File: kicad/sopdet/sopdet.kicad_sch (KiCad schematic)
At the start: 0 parts

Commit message: Finish Sopdet schematic
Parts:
- added C1: 10u, Capacitor_SMD:C_0603_1608Metric_Pad1.08x0.95mm_HandSolder, symbol Device:C_Small
- added C10, C2, C3, C9: 0, Capacitor_SMD:C_0603_1608Metric, symbol Device:C_Small
- added C11, C12: 100p, Capacitor_SMD:C_0603_1608Metric, symbol Device:C_Small
- added C13, C15: 100n, Capacitor_SMD:C_0603_1608Metric, symbol Device:C_Small
- added C14: 10u, Capacitor_SMD:C_0603_1608Metric, symbol Device:C_Small
- added C16: 33p, Capacitor_SMD:C_0603_1608Metric, symbol Device:C_Small
- added C4: 100n, Capacitor_SMD:C_0603_1608Metric_Pad1.08x0.95mm_HandSolder, symbol Device:C_Small
- added C5: 47p, Capacitor_SMD:C_0603_1608Metric_Pad1.08x0.95mm_HandSolder, symbol Device:C_Small
- added C6, C7: 22u, Capacitor_SMD:C_1206_3216Metric, symbol Device:C_Small
- added C8: 1000u, Capacitor_SMD:CP_Elec_10x10.5, symbol Device:C_Polarized_Small
- added D1, D2: LED_Small, LED_SMD:LED_0603_1608Metric_Pad1.05x0.95mm_HandSolder, symbol Device:LED_Small
- added D3: TVS, Diode_SMD:D_SOD-882, symbol Diode:PTVS5V0Z1USK
- added D4: Blue LED, LED_SMD:LED_0603_1608Metric_Pad1.05x0.95mm_HandSolder, symbol Device:LED
- added D5: Yellow LED, LED_SMD:LED_0603_1608Metric_Pad1.05x0.95mm_HandSolder, symbol Device:LED
- added D6: Orange LED, LED_SMD:LED_0603_1608Metric_Pad1.05x0.95mm_HandSolder, symbol Device:LED
- added J1, J2: IPEX_MHF1, sirius:ipex_mhf1, symbol sirius:IPEX_MHF1
- added L1: 6.8u, sirius:1277AS-H-1R0M=P2, symbol Device:L_Small
- added L2: 68n, Inductor_SMD:L_0603_1608Metric, symbol Device:L_Small
- added Q1: Q_PMOS_GSD, sirius:SOT_7DS-T1-GE3_VIS, symbol Transistor_FET:Q_PMOS_GSD
- added R1, R5: 0, Resistor_SMD:R_0603_1608Metric, symbol Device:R_Small
- added R10, R7: 1k, Resistor_SMD:R_0603_1608Metric_Pad0.98x0.95mm_HandSolder, symbol Device:R_Small
- added R11, R12, R9: 1k, Resistor_SMD:R_0603_1608Metric, symbol Device:R_Small
- added R2: 2k, Resistor_SMD:R_0603_1608Metric_Pad0.98x0.95mm_HandSolder, symbol Device:R_Small
- added R3: 158k, Resistor_SMD:R_0603_1608Metric_Pad0.98x0.95mm_HandSolder, symbol Device:R_Small
- added R4: 30.1k, Resistor_SMD:R_0603_1608Metric_Pad0.98x0.95mm_HandSolder, symbol Device:R_Small
- added R6: 10r, Resistor_SMD:R_0603_1608Metric, symbol Device:R_Small
- added R8: 5.6k, Resistor_SMD:R_0603_1608Metric_Pad0.98x0.95mm_HandSolder, symbol Device:R_Small
- added U1: Power_Connector, sirius:XT60, symbol sirius:XT60
- added U2: AP63301WU-7, sirius:SOT95P280X100-6N, symbol sirius:AP63300WU-7
- added U3: RFM95W-915S2, sirius:RFM95W-915S2, symbol sirius:RFM95W-915S2
- added U4: LC29H (DA), sirius:LC29H, symbol sirius:LC29H (DA)
- added U5: Pi Zero 2W, sirius:Pi_hat_generic, symbol sirius:Pi_Zero_2W
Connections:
- new net: D1.1 (K), D2.2 (A), R2.2
- new net: C2.1, J1.1, R1.1
- new net: C10.2, C11.1, R5.2
- new net: D5.2 (A), R12.1
- new net: C11.2, D3.1 (K), J2.1, L2.1
- new net: C12.1, C13.1, L2.2, R6.1
- new net: D6.2 (A), R9.2
- new net: C4.2, L1.1, U2.5 (SW)
- new net: R7.2, U4.20 (TXD1)
- new net: D4.2 (A), R11.1
- new net: C5.2, R3.2, R4.1, U2.1 (FB)
- new net: C3.1, R1.2, U3.9 (ANT)
- new net: C4.1, U2.6 (BST)
- new net +3V3: C14.2, C15.2, C16.2, R11.2, R12.2, U3.13 (3.3V), U4.22 (V_BCKP), U4.23 (VCC), U5.1 (3V3_1), U5.17 (3V3_17)
- new net +5V: C5.1, C6.1, C7.1, L1.2, R3.1, U5.2 (5V_2), U5.4 (5V_4)
- new net +BATT: Q1.3 (D), R2.1, U1.1 (Vin)
- new net CS0_SPI0: U3.5 (NSS), U5.24 (GPIO8/SPI_~{CE0})
- new net GND: C1.2, C10.1, C12.2, C13.2, C14.1, C15.1, C16.1, C2.2, C3.2, C6.2, C7.2, C8.2, C9.1, D1.2 (A), D2.1 (K), D3.2 (A), D6.1 (K), J1.2, J1.3, J2.2, J2.3, Q1.1 (G), R4.2, R8.2, U1.2 (Ground), U2.4 (GND), U3.1 (GND), U3.10 (GND), U3.8 (GND), U4.10 (GND), U4.12 (GND__1), U4.13 (GND__2), U4.24 (GND__3), U5.14 (GND_14), U5.20 (GND_20), U5.25 (GND_25), U5.30 (GND_30), U5.34 (GND_34), U5.39 (GND_39), U5.6 (GND_6), U5.9 (GND_9)
- new net GPIO25: U3.14 (DIO0), U5.22 (GPIO25/GPIO_GEN6)
- new net GPIO26: U3.16 (DIO2), U5.37 (GPIO26)
- new net GPIO6: U3.15 (DIO1), U5.31 (GPIO6)
- new net MISO_SPI0: U3.2 (MISO), U5.21 (GPIO9/SPI_MISO)
- new net MOSI_SPI0: U3.3 (MOSI), U5.19 (GPIO10/SPI_MOSI)
- new net PPS: R9.1, U4.3 (1PPS)
- new net Pi_RX: D4.1 (K), R7.1, U5.10 (GPIO15/RXD0)
- new net Pi_TX: D5.1 (K), R10.2, U5.8 (GPIO14/TXD0)
- new net Pi_TX_2_8: R10.1, R8.1, U4.21 (RXD1)
- new net RESET: U3.6 (RESET), U5.11 (GPIO17/GPIO_GEN0)
- new net RF_IN: C9.2, R5.1, U4.11 (RF_IN)
- new net SCK_SPI0: U3.4 (SCK), U5.23 (GPIO11/SPI_SCLK)
- new net VCC: C1.1, C8.1, Q1.2 (S), U2.2 (EN), U2.3 (VIN)
- new net VDD_RF: R6.2, U4.9 (VDD_RF)
- no-connect marks 0 -> 30
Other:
- note added: "Activity Indicators"
- note added: "Bulk Capacitor"
- note added: "LC29H(DA)"
- note added: "Level Shifting"
- note added: "POWER"
- note added: "Pi Zero 2W"
- note added: "Power LED"
- note added: "RASPBERRY PI"
- note added: "RF"
- note added: "RFM95-915S2"
- note added: "RP Protection"
- note added: "Voltage Regulator"
- note added: "XT60 Power Connector"
- title: (none) -> Sopdet

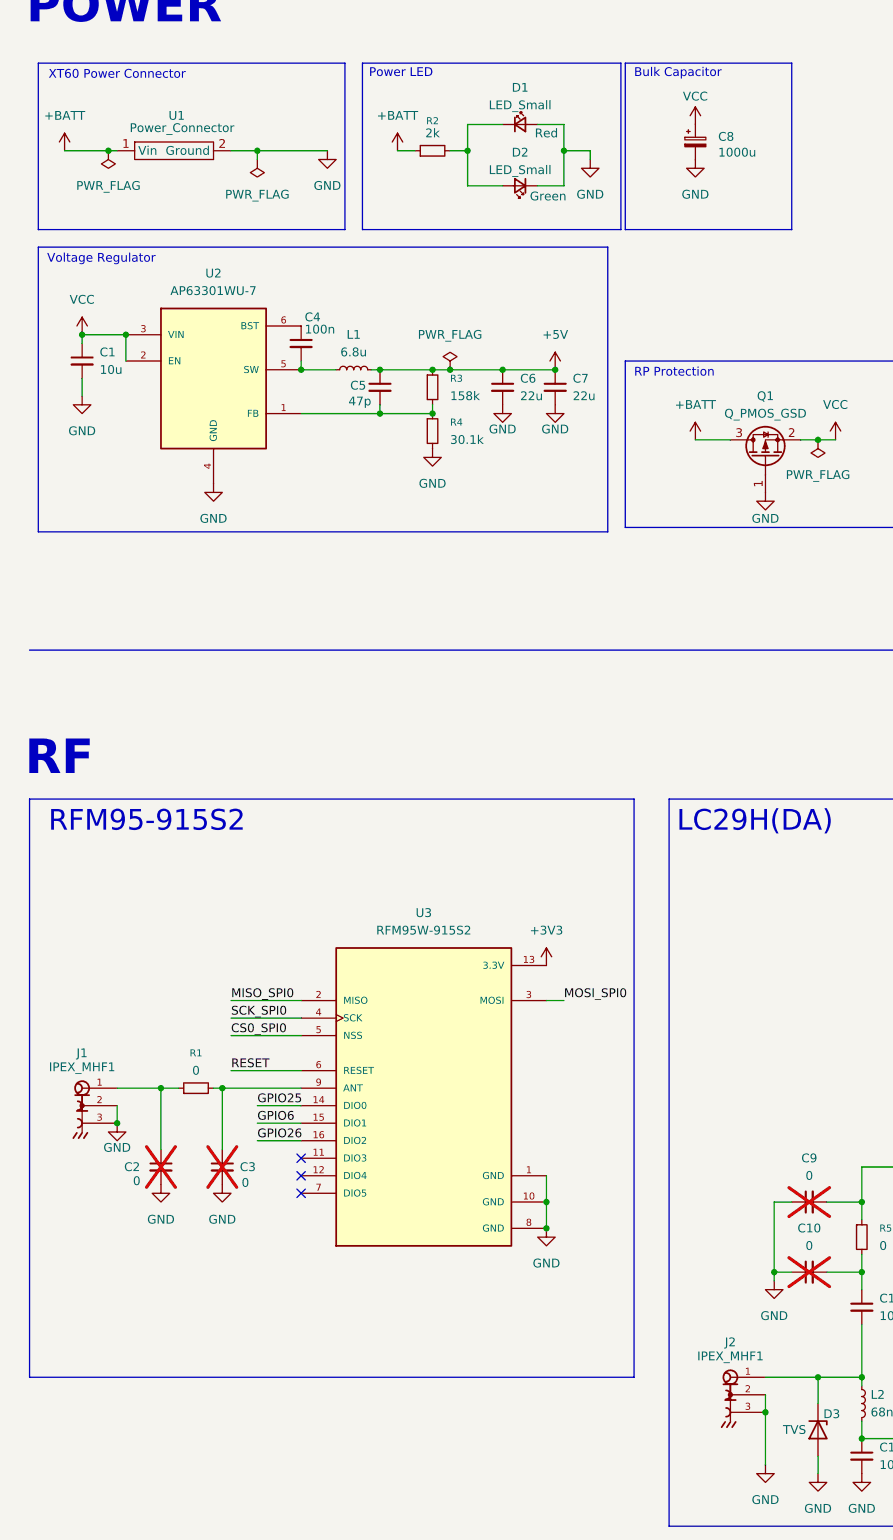
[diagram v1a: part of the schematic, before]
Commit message: Replace footprint of u.fl connector & screw terminal
Redesign board to accomodate larger footprint, make Sopdet a little smaller to qualify for $2 jlcpcb price, assign Digikey PN to all components, add a script which combines the BOM's of both boards so Digikey can more accurately detect cost savings
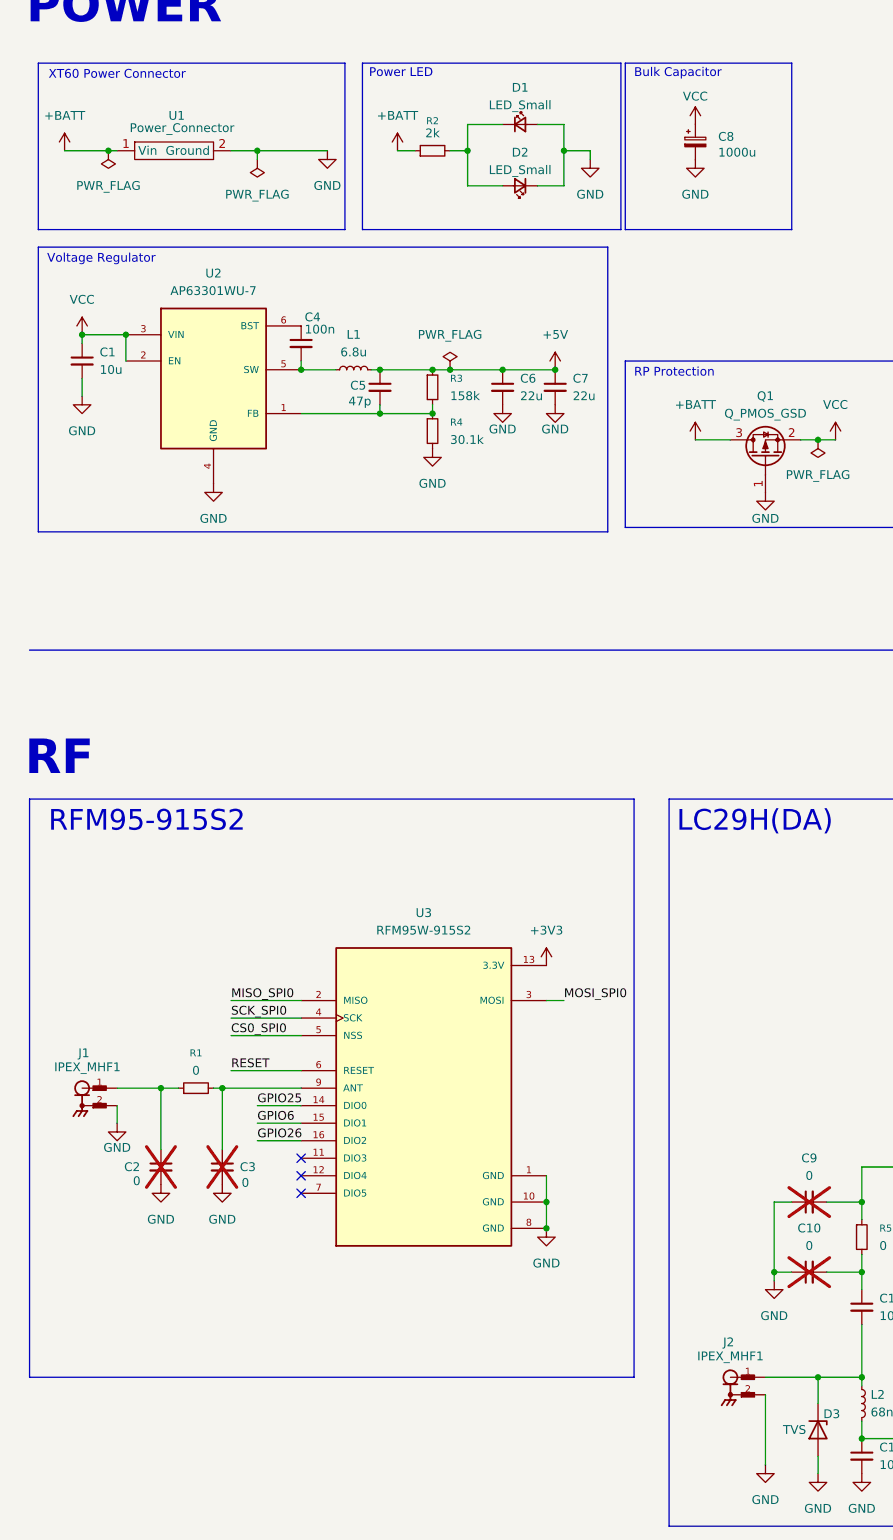
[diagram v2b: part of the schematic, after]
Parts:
- C1, C14: Digikey PN (none) -> 587-3258-1-ND
- C11, C12: Digikey PN (none) -> 490-1427-1-ND
- C13, C15, C4: Digikey PN (none) -> 399-C0603C104K3RACTUCT-ND
- C16: Digikey PN (none) -> 1276-1070-1-ND
- C5: Digikey PN (none) -> 1276-1037-1-ND
- C6, C7: Digikey PN (none) -> 587-3246-1-ND
- C8: Digikey PN (none) -> 565-HHXJ160ARA102MJC5GCT-ND
- D1: Color Red -> (none)
- D2: Color Green -> (none)
- J1, J2: footprint sirius:ipex_mhf1 -> sirius:TE_CONMHF1-SMD-T; symbol sirius:IPEX_MHF1 -> sirius:CONMHF1-SMD-T; Digikey PN (none) -> 343-CONMHF1-SMD-TCT-ND
- L2: Digikey PN (none) -> 490-1178-1-ND
- R1, R5: Digikey PN (none) -> 311-0.0GRCT-ND
- R10, R11, R12, R7, R9: Digikey PN (none) -> RMCF0603FT1K00CT-ND
- R3: Digikey PN (none) -> 311-158KHRCT-ND
- R4: Digikey PN (none) -> RMCF0603FT30K1CT-ND
- R6: Digikey PN (none) -> RMCF0603FT10R0CT-ND
- R8: Digikey PN (none) -> 311-5.60KHRCT-ND
- U3: AVAILABILITY Unavailable -> (none); Availability In Stock -> (none); Check_prices https://www.snapeda.com/parts/RFM95W-915S2/RF/view-part/?re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 -> (none); Description_1 802.15.4 LoRa™ Transceiver Module 915MHz Antenna Not Includ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 -> (none); MF RF Solutions -> (none); MP RFM95W-915S2 -> (none); PACKAGE SMD-16 RF Solutions -> (none); PRICE None -> (none); Package Non Standard RF Solutions -> (none); Price None -> (none); STANDARD Manufacturer recommendations -> (none); SnapEDA_Link https://www.snapeda.com/parts/RFM95W-915S2/RF/view-part/?re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 -> (none)
- U4: Digikey PN (none) -> 2958-LC29HDAMDCT-ND
- U5: Availability In Stock -> (none); Check_prices https://www.snapeda.com/parts/RASPBERRY%20PI%20ZERO%202%20W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 -> (none); Description_1 At the heart of Raspberry Pi Zero 2 W is RP3A0, a custom-bu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 -> (none); MANUFACTURER Raspberry Pi -> (none); MF Raspberry Pi -> (none); MP RASPBERRY PI ZERO 2 W -> (none); PARTREV April 2024 -> (none); Package None -> (none); Price None -> (none); STANDARD Manufacturer Recommendations -> (none); SnapEDA_Link https://www.snapeda.com/parts/RASPBERRY%20PI%20ZERO%202%20W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 -> (none)
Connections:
- net GND: now also J1.4, J2.4
